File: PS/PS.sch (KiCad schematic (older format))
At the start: 53 parts, among them J1 Conn_01x01, J10 Conn_01x01, J11 Conn_01x01, J12 Conn_01x01, J13 Conn_01x01, J14 Conn_01x01, J15 Conn_01x01, J2 Conn_01x01, J3 Conn_01x03, J4 Conn_01x01, J5 Conn_01x01, J6 Conn_01x01, J7 Conn_01x01, J8 Conn_01x01, J9 Conn_01x01, Q1 BCP56, Q10 BC848, Q2 BCP56, Q3 BCP56, Q4 BCP56, Q5 BCP56, Q6 BCP56, Q7 BCP56, Q8 BCP56, Q9 BCP56, U1 LM358, U2 LM358, U3 LM358, U4 LM358, U5 LM358

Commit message: Shared libraries
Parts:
- D56: value BZT52Bxx -> 2.4
- Q1, Q2, Q3, Q4, Q5, Q6, Q7, Q8, Q9: symbol Library:BCP56 -> Lighttable:BCP56
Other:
- note removed: "2.4V"
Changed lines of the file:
@@
 P 8200 4550
 F 0 "D56" V 8154 4630 50  0000 L CNN
-F 1 "BZT52Bxx" V 8245 4630 50  0000 L CNN
+F 1 "2.4" V 8245 4630 50  0000 L CNN
 F 2 "Diode_SMD:D_SOD-123" H 8200 4375 50  0001 C CNN
 F 3 "https://diotec.com/tl_files/diotec/files/pdf/datasheets/bzt52b2v4.pdf" H 8200 4550 50  0001 C CNN
@@
 	8700 2950 8700 2850
 Connection ~ 8700 2850
-Text Notes 8050 4600 2    50   ~ 0
-2.4V
 $Comp
 L Connector_Generic:Conn_01x01 J1
@@
 	2000 1900 2000 1800
 $Comp
-L Library:BCP56 Q1
+L Lighttable:BCP56 Q1
 U 1 1 61B847FA
 P 1900 2100
@@
 $EndComp
 $Comp
-L Library:BCP56 Q4
+L Lighttable:BCP56 Q4
 U 1 1 61B89CE5
 P 3300 2100
@@
 $EndComp
 $Comp
-L Library:BCP56 Q6
+L Lighttable:BCP56 Q6
 U 1 1 61B8B288
 P 4700 2100
@@
 $EndComp
 $Comp
-L Library:BCP56 Q8
+L Lighttable:BCP56 Q8
 U 1 1 61B8CF98
 P 6100 2100
@@
 $EndComp
 $Comp
-L Library:BCP56 Q9
+L Lighttable:BCP56 Q9
 U 1 1 61B8EA14
 P 7500 2100
@@
 $EndComp
 $Comp
-L Library:BCP56 Q2
+L Lighttable:BCP56 Q2
 U 1 1 61B900A2
 P 1850 4250
@@
 $EndComp
 $Comp
-L Library:BCP56 Q3
+L Lighttable:BCP56 Q3
 U 1 1 61B91BCF
 P 3250 4250
@@
 $EndComp
 $Comp
-L Library:BCP56 Q5
+L Lighttable:BCP56 Q5
 U 1 1 61B9325E
 P 4650 4250
@@
 $EndComp
 $Comp
-L Library:BCP56 Q7
+L Lighttable:BCP56 Q7
 U 1 1 61B94A0B
 P 6050 4250

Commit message: Incorrect value
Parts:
- R14: value 3k -> 150k
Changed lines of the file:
@@
 P 8550 4300
 F 0 "R14" V 8343 4300 50  0000 C CNN
-F 1 "3k" V 8434 4300 50  0000 C CNN
+F 1 "150k" V 8434 4300 50  0000 C CNN
 F 2 "Resistor_SMD:R_0805_2012Metric" V 8480 4300 50  0001 C CNN
 F 3 "~" H 8550 4300 50  0001 C CNN

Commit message: Vce saturation voltage is too hight, use MOSFET as a switch
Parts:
- Q10: value BC848 -> 2N7002; symbol Transistor_BJT:BC848 -> Transistor_FET:2N7002
- R15: value 10k -> 100
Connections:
- net C1: now reaches J7.1 (Pin_1), Q1.4 (C)
- net C2: now reaches J9.1 (Pin_1), Q4.4 (C)
- net C3: now reaches J11.1 (Pin_1), Q6.4 (C)
- net C4: now reaches J13.1 (Pin_1), Q8.4 (C)
- net C5: now reaches J14.1 (Pin_1), Q9.4 (C)
- net C6: now reaches J6.1 (Pin_1), Q2.4 (C)
- net C7: now reaches J8.1 (Pin_1), Q3.4 (C)
- net C8: now reaches J10.1 (Pin_1), Q5.4 (C)
- net C9: now reaches J12.1 (Pin_1), Q7.4 (C)
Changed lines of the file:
@@
 	6600 2000 6650 2000
 $Comp
-L Transistor_BJT:BC848 Q10
+L Transistor_FET:2N7002 Q10
 U 1 1 61AD3420
 P 8950 5250
 F 0 "Q10" H 9141 5296 50  0000 L CNN
-F 1 "BC848" H 9141 5205 50  0000 L CNN
+F 1 "2N7002" H 9141 5205 50  0000 L CNN
 F 2 "Package_TO_SOT_SMD:SOT-23" H 9150 5175 50  0001 L CIN
-F 3 "http://www.infineon.com/dgdl/Infineon-BC847SERIES_BC848SERIES_BC849SERIES_BC850SERIES-DS-v01_01-en.pdf?fileId=db3a304314dca389011541d4630a1657" H 8950 5250 50  0001 L CNN
+F 3 "https://www.onsemi.com/pub/Collateral/NDS7002A-D.PDF" H 8950 5250 50  0001 L CNN
 	1    8950 5250
 	1    0    0    -1
@@
 P 8500 5250
 F 0 "R15" V 8293 5250 50  0000 C CNN
-F 1 "10k" V 8384 5250 50  0000 C CNN
+F 1 "100" V 8384 5250 50  0000 C CNN
 F 2 "Resistor_SMD:R_0805_2012Metric" V 8430 5250 50  0001 C CNN
 F 3 "~" H 8500 5250 50  0001 C CNN
@@
 $EndComp
 Wire Wire Line
-	1950 3900 1950 4050
+	1950 3900 1950 3950
 $Comp
 L Connector_Generic:Conn_01x01 J15
@@
 Connection ~ 7250 4300
 Wire Wire Line
-	2000 1900 2000 1800
+	2000 1900 2000 1850
 $Comp
 L Lighttable:BCP56 Q1
@@
 $EndComp
 Wire Wire Line
-	6150 3900 6150 4050
-Wire Wire Line
-	4750 3900 4750 4050
-Wire Wire Line
-	3350 3900 3350 4050
-Wire Wire Line
-	3400 1800 3400 1900
-Wire Wire Line
-	4800 1800 4800 1900
-Wire Wire Line
-	6200 1800 6200 1900
-Wire Wire Line
-	7600 1800 7600 1900
+	6150 3900 6150 3950
+Wire Wire Line
+	4750 3900 4750 3950
+Wire Wire Line
+	3350 3900 3350 3950
+Wire Wire Line
+	3400 1800 3400 1850
+Wire Wire Line
+	4800 1800 4800 1850
+Wire Wire Line
+	6200 1800 6200 1850
+Wire Wire Line
+	7600 1800 7600 1850
 $Comp
 L Mechanical:MountingHole H1
@@
 	0    -1   -1   0
 $EndComp
+Text Label 2050 1850 0    50   ~ 0
+C1
+Wire Wire Line
+	2050 1850 2000 1850
+Connection ~ 2000 1850
+Wire Wire Line
+	2000 1850 2000 1800
+Text Label 3450 1850 0    50   ~ 0
+C2
+Wire Wire Line
+	3450 1850 3400 1850
+Connection ~ 3400 1850
+Wire Wire Line
+	3400 1850 3400 1900
+Text Label 4850 1850 0    50   ~ 0
+C3
+Wire Wire Line
+	4850 1850 4800 1850
+Connection ~ 4800 1850
+Wire Wire Line
+	4800 1850 4800 1900
+Text Label 6250 1850 0    50   ~ 0
+C4
+Wire Wire Line
+	6250 1850 6200 1850
+Connection ~ 6200 1850
+Wire Wire Line
+	6200 1850 6200 1900
+Text Label 7650 1850 0    50   ~ 0
+C5
+Wire Wire Line
+	7650 1850 7600 1850
+Connection ~ 7600 1850
+Wire Wire Line
+	7600 1850 7600 1900
+Text Label 2000 3950 0    50   ~ 0
+C6
+Wire Wire Line
+	2000 3950 1950 3950
+Connection ~ 1950 3950
+Wire Wire Line
+	1950 3950 1950 4050
+Text Label 3400 3950 0    50   ~ 0
+C7
+Wire Wire Line
+	3400 3950 3350 3950
+Connection ~ 3350 3950
+Wire Wire Line
+	3350 3950 3350 4050
+Text Label 4800 3950 0    50   ~ 0
+C8
+Wire Wire Line
+	4800 3950 4750 3950
+Connection ~ 4750 3950
+Wire Wire Line
+	4750 3950 4750 4050
+Text Label 6200 3950 0    50   ~ 0
+C9
+Wire Wire Line
+	6200 3950 6150 3950
+Connection ~ 6150 3950
+Wire Wire Line
+	6150 3950 6150 4050
 $EndSCHEMATC

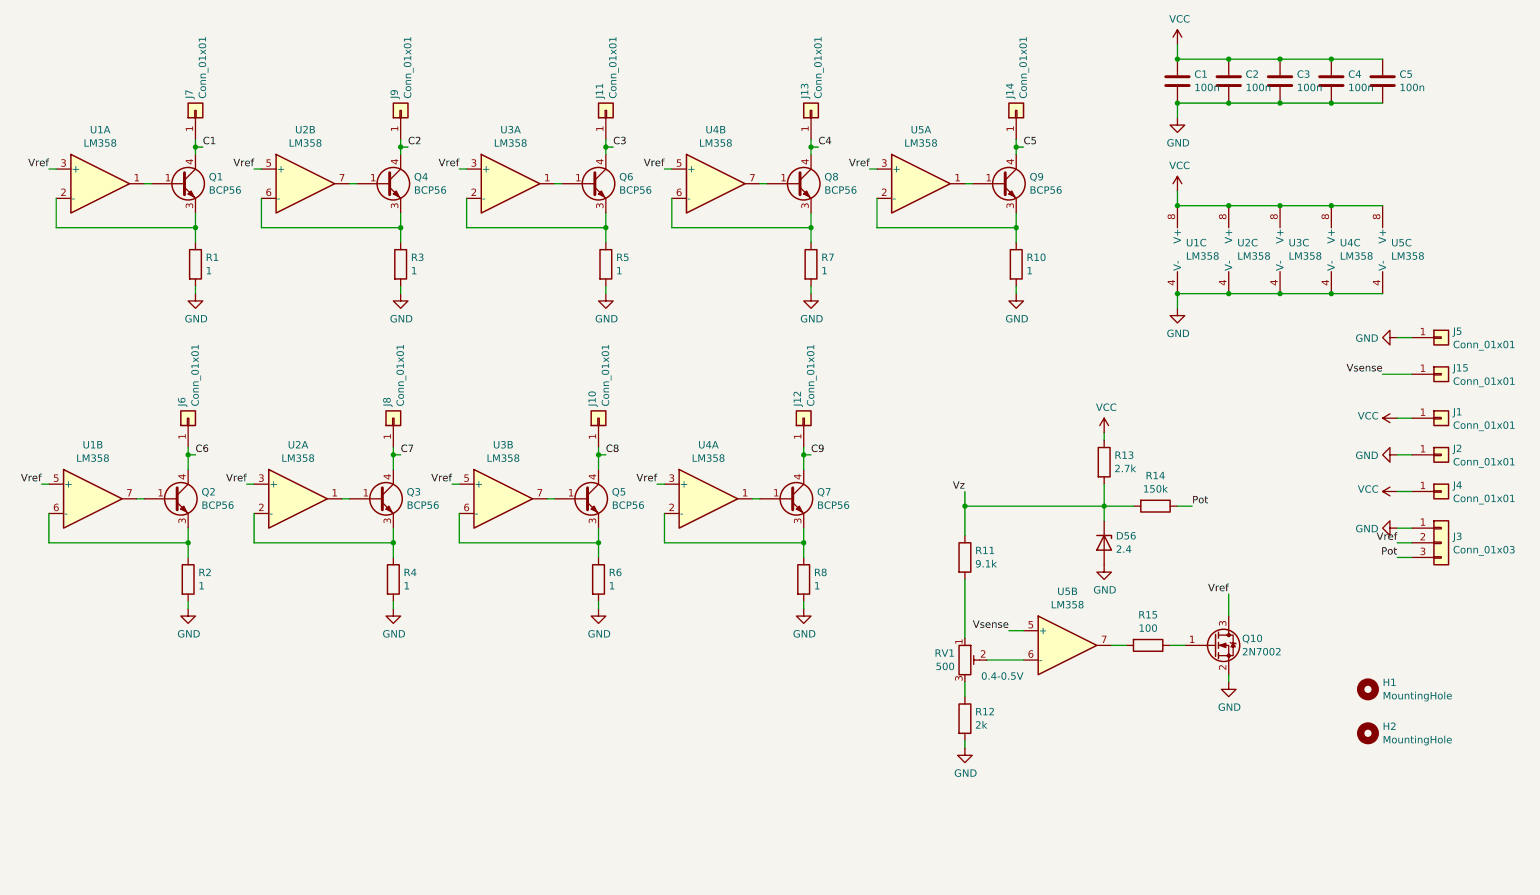
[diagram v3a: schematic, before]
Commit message: More fixes (magic smoke happened)
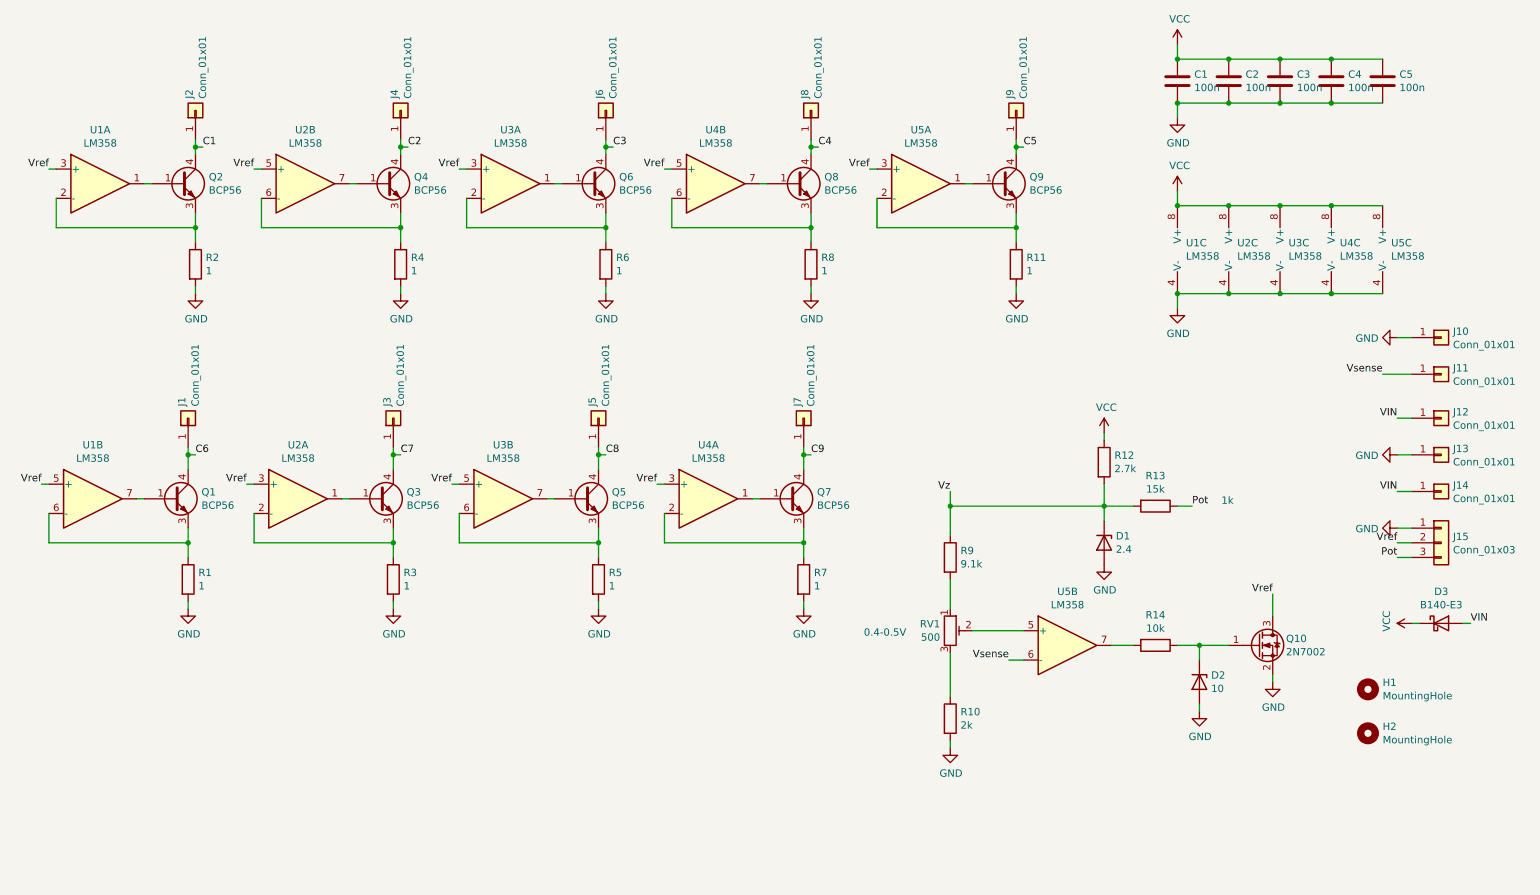
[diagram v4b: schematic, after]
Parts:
- added D2: 10, Diode_SMD:D_SOD-123, symbol Diode:BZT52Bxx
- added D3: B140-E3, Diode_SMD:D_SMA, symbol Diode:B140-E3
- R13: renamed from R14; value 150k -> 15k
- R14: renamed from R15; value 100 -> 10k
- renumbered D56 to D1, J6 to J1, J5 to J10, J15 to J11, J1 to J12, J2 to J13, J4 to J14, J3 to J15, J7 to J2, J8 to J3, J9 to J4, J10 to J5, J11 to J6, J12 to J7, J13 to J8, J14 to J9, Q2 to Q1, Q1 to Q2, R2 to R1, R12 to R10, R10 to R11, R13 to R12, R1 to R2, R4 to R3, R3 to R4, R6 to R5, R5 to R6, R8 to R7, R7 to R8, R11 to R9
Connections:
- net GND: now also D2.2 (A)
- net VCC: now also D3.1 (K); no longer J12.1 (Pin_1), J14.1 (Pin_1)
- net Vsense: now also U5.6 (-); no longer U5.5 (+)
- net at Q10.1 (G), R14.1: now also D2.1 (K)
- net at RV1.2: now also U5.5 (+); no longer U5.6 (-)
- new net VIN: D3.2 (A), J12.1 (Pin_1), J14.1 (Pin_1)
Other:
- note added: "1k"
- moved on the sheet: Q10, R10, R14, R9, RV1

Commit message: protect sense input
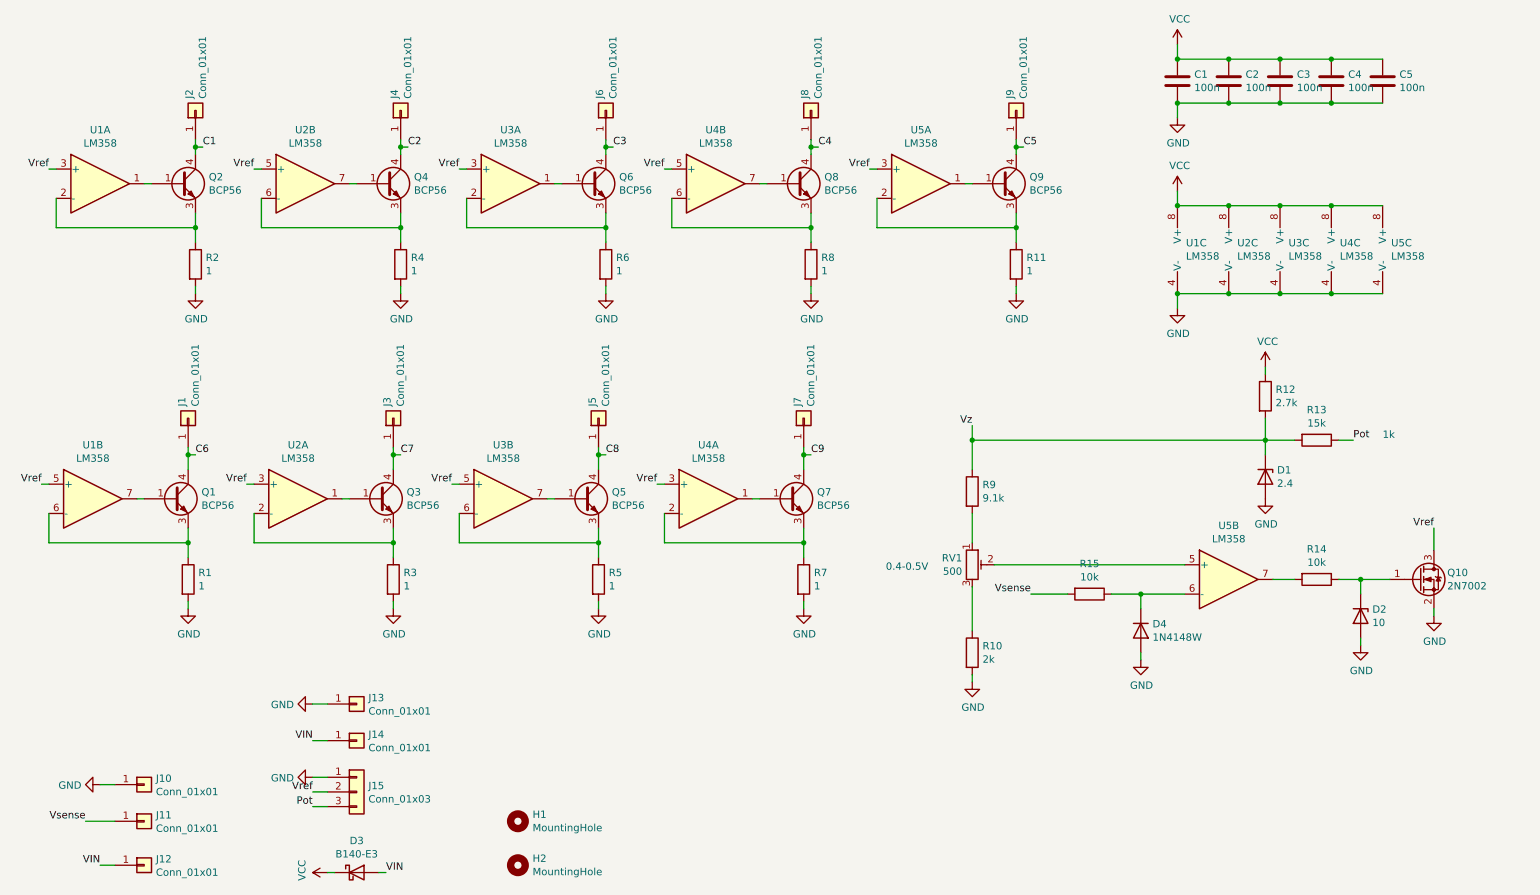
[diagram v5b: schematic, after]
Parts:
- added D4: 1N4148W, Diode_SMD:D_SOD-123, symbol Diode:1N4148W
- added R15: 10k, Resistor_SMD:R_0805_2012Metric, symbol Device:R
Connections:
- net GND: now also D4.2 (A)
- net Vsense: now also R15.2; no longer U5.6 (-)
- new net: D4.1 (K), R15.1, U5.6 (-)
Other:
- moved on the sheet: D1, D2, D3, H1, H2, J10, J11, J12, J13, J14, J15, Q10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
